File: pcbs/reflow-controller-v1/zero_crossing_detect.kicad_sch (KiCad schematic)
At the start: 13 parts, among them Q1601 MMBT3904, Q1602 140357145200

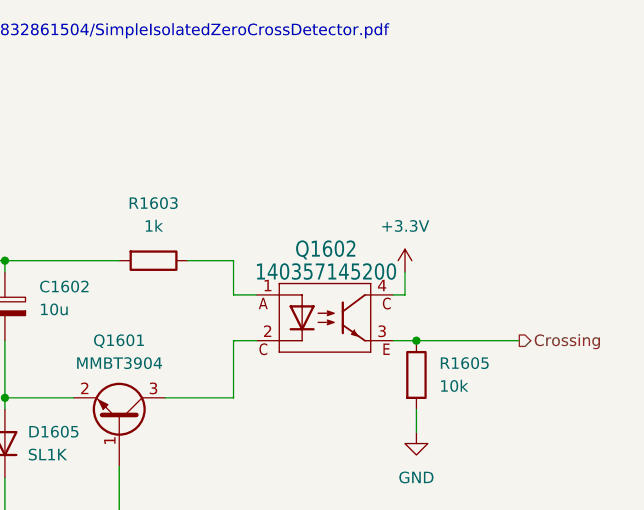
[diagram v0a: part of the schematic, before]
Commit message: fix zero crossing detector 3.3 voltage supply
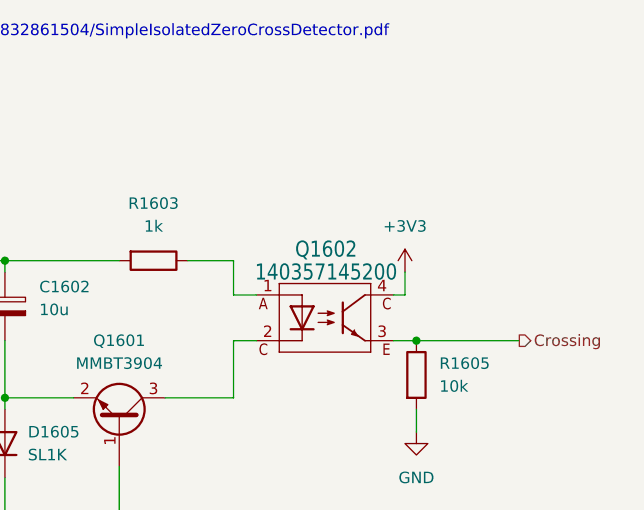
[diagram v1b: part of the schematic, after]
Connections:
- net +3.3V renamed +3V3
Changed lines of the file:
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@@
-	)
-	(symbol
-		(lib_id "power:+3.3V")
-		(at 157.48 43.18 0)
-		(unit 1)
-		(exclude_from_sim no)
-		(in_bom yes)
-		(on_board yes)
-		(dnp no)
-		(fields_autoplaced yes)
-		(property "Reference" "#PWR01601"
-			(at 157.48 46.99 0)
-			(effects
-				(font
-					(size 1.27 1.27)
-				)
-				(hide yes)
-			)
-		)
-		(property "Value" "+3.3V"
-			(at 157.48 38.1 0)
-			(effects
-				(font
-					(size 1.27 1.27)
-				)
-			)
-		)
-		(property "Footprint" ""
-			(at 157.48 43.18 0)
-			(effects
-				(font
-					(size 1.27 1.27)
-				)
-				(hide yes)
-			)
-		)
-		(property "Datasheet" ""
-			(at 157.48 43.18 0)
-			(effects
-				(font
-					(size 1.27 1.27)
-				)
-				(hide yes)
-			)
-		)
-		(property "Description" "Power symbol creates a global label with name \"+3.3V\""
-			(at 157.48 43.18 0)
-			(effects
-				(font
-					(size 1.27 1.27)
-				)
-				(hide yes)
-			)
-		)
-		(pin "1"
-		)
-		(instances
-			(project ""
-				(path "/843848ae-bf49-42cb-8f8b-76790d2e568d/750e63f5-dc4e-4e64-b2d6-60412c57ffed"
-					(reference "#PWR01601")
-					(unit 1)
-				)
-			)
-		)
 	)
 	(symbol
@@
 					(unit 1)
 				)
+			)
+		)
+	)
+	(symbol
+		(lib_id "power:+3V3")
+		(at 157.48 43.18 0)
+		(unit 1)
+		(exclude_from_sim no)
+		(in_bom yes)
+		(on_board yes)
+		(dnp no)
+		(fields_autoplaced yes)
+		(property "Reference" "#PWR01601"
+			(at 157.48 46.99 0)
+			(effects
+				(font
+					(size 1.27 1.27)
+				)
+				(hide yes)
+			)
+		)
+		(property "Value" "+3V3"
+			(at 157.48 38.1 0)
+			(effects
+				(font
+					(size 1.27 1.27)
+				)
+			)
+		)
+		(property "Footprint" ""
+			(at 157.48 43.18 0)
+			(effects
+				(font
+					(size 1.27 1.27)
+				)
+				(hide yes)
+			)
+		)
+		(property "Datasheet" ""
+			(at 157.48 43.18 0)
+			(effects
+				(font
+					(size 1.27 1.27)
+				)
+				(hide yes)
+			)
+		)
+		(property "Description" "Power symbol creates a global label with name \"+3V3\""
+			(at 157.48 43.18 0)
+			(effects
+				(font
+					(size 1.27 1.27)
+				)
+				(hide yes)
+			)
+		)
+		(pin "1"
+		)
+		(instances
+			(project ""
+				(path "/843848ae-bf49-42cb-8f8b-76790d2e568d/750e63f5-dc4e-4e64-b2d6-60412c57ffed"
+					(reference "#PWR01601")
+					(unit 1)
+				)

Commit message: update display placing & prelim. routing
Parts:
- Q1602: footprint wuerth:WL-OCPT_SOP4 -> WL-OCPT_LSOP4
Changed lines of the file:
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@@
 			)
 		)
-		(property "Datasheet" ""
+		(property "Datasheet" "~"
 			(at 113.03 46.99 0)
 			(effects
@@
 			)
 		)
-		(property "Datasheet" "https://diotec.com/request/datasheet/sl1a.pdf"
+		(property "Datasheet" "~"
 			(at 93.98 52.07 0)
 			(effects
@@
 			)
 		)
-		(property "Footprint" "wuerth:WL-OCPT_SOP4"
+		(property "Footprint" "WL-OCPT_LSOP4"
 			(at 149.098 54.356 0)
 			(effects
@@
 			)
 		)
-		(property "Datasheet" "https://diotec.com/request/datasheet/sl1a.pdf"
+		(property "Datasheet" "~"
 			(at 93.98 72.39 0)
 			(effects
@@
 			)
 		)
-		(property "Datasheet" "https://diotec.com/request/datasheet/sl1a.pdf"
+		(property "Datasheet" "~"
 			(at 113.03 62.23 0)
 			(effects
@@
 			)
 		)
-		(property "Datasheet" "https://diotec.com/request/datasheet/sl1a.pdf"
+		(property "Datasheet" "~"
 			(at 93.98 41.91 0)
 			(effects
@@
 			)
 		)
-		(property "Datasheet" "https://diotec.com/request/datasheet/sl1a.pdf"
+		(property "Datasheet" "~"
 			(at 93.98 63.5 0)
 			(effects
